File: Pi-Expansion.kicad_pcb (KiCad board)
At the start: 2 copper layers, 56 x 65 mm, 129 parts, among them J1 RPi_GPIO, J2 MMCX_H, J3 PINHEADER_2X2_SMD, P1 BATT, U1 A2200-A, U2 Racom R-78B5.0-1.5L

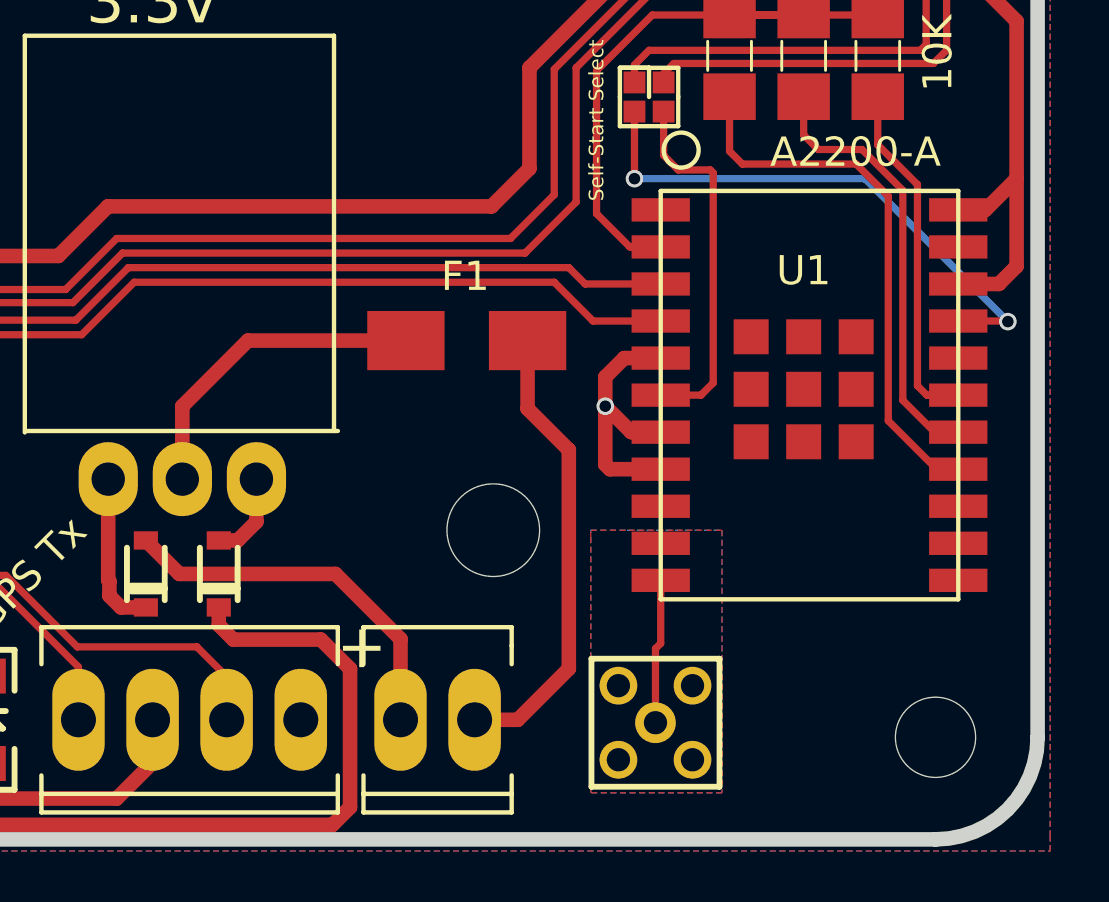
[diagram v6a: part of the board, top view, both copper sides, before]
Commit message: Added voltage select for GPS Vant between 5v and 3v3.
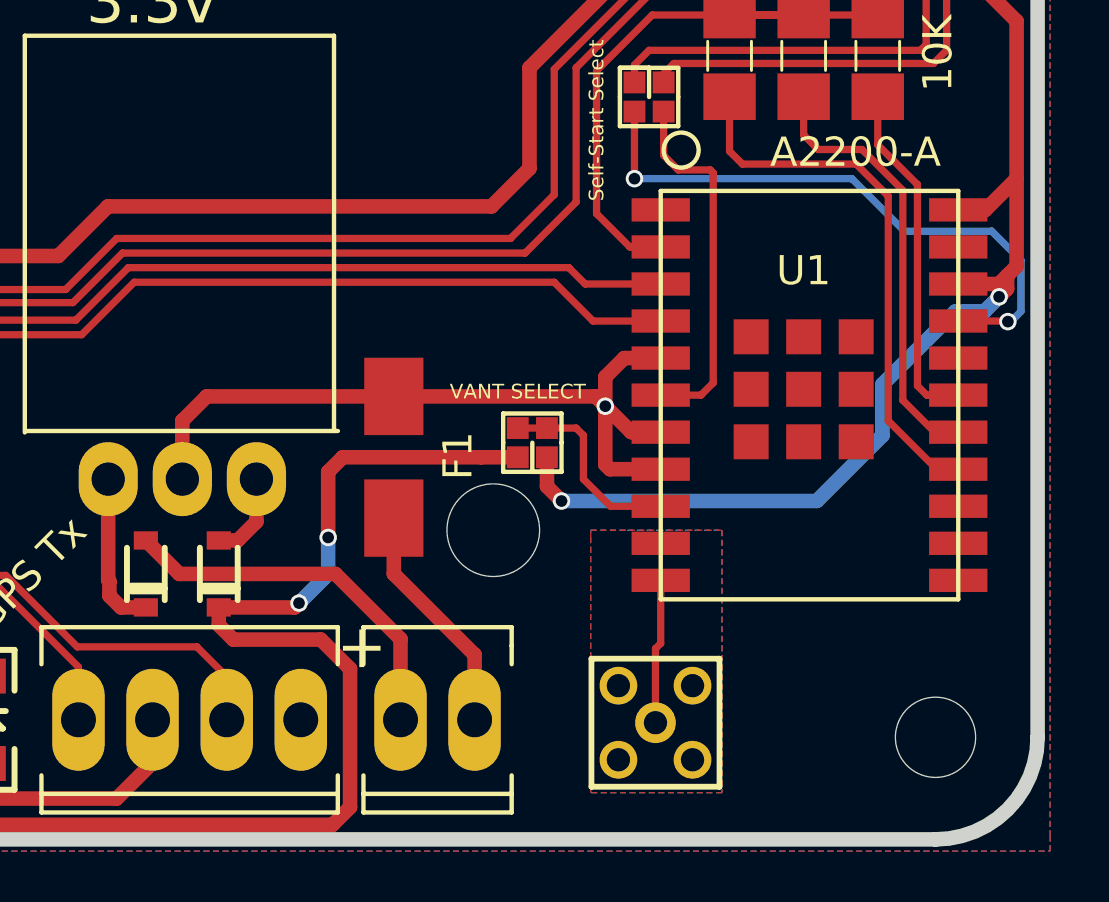
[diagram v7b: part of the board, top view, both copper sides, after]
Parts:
- added J4: PINHEADER_2X2_SMD, Sailbot_Custom:2-WAY-SMD-JUMPER, F.Cu at (106.8, 124.0)
- moved F1 4.72 mm to (102.0, 124.5), turned to 270 degrees
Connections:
- U1 pad 9: (no net) -> Net-(J4-Pad2)
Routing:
- net +3V3: track 143.7 -> 165.1 mm, vias 0 -> 2
- net +5V: track 135.3 -> 149.7 mm, vias 0 -> 2
- net Net-(F1-Pad2): track 15.8 -> 8.06 mm
- net Net-(J4-Pad2): track 0.00 -> 6.89 mm
- net GND: track 56.3 -> 62.2 mm
- net Net-(J3-Pad4): track 18.8 -> 20.8 mm

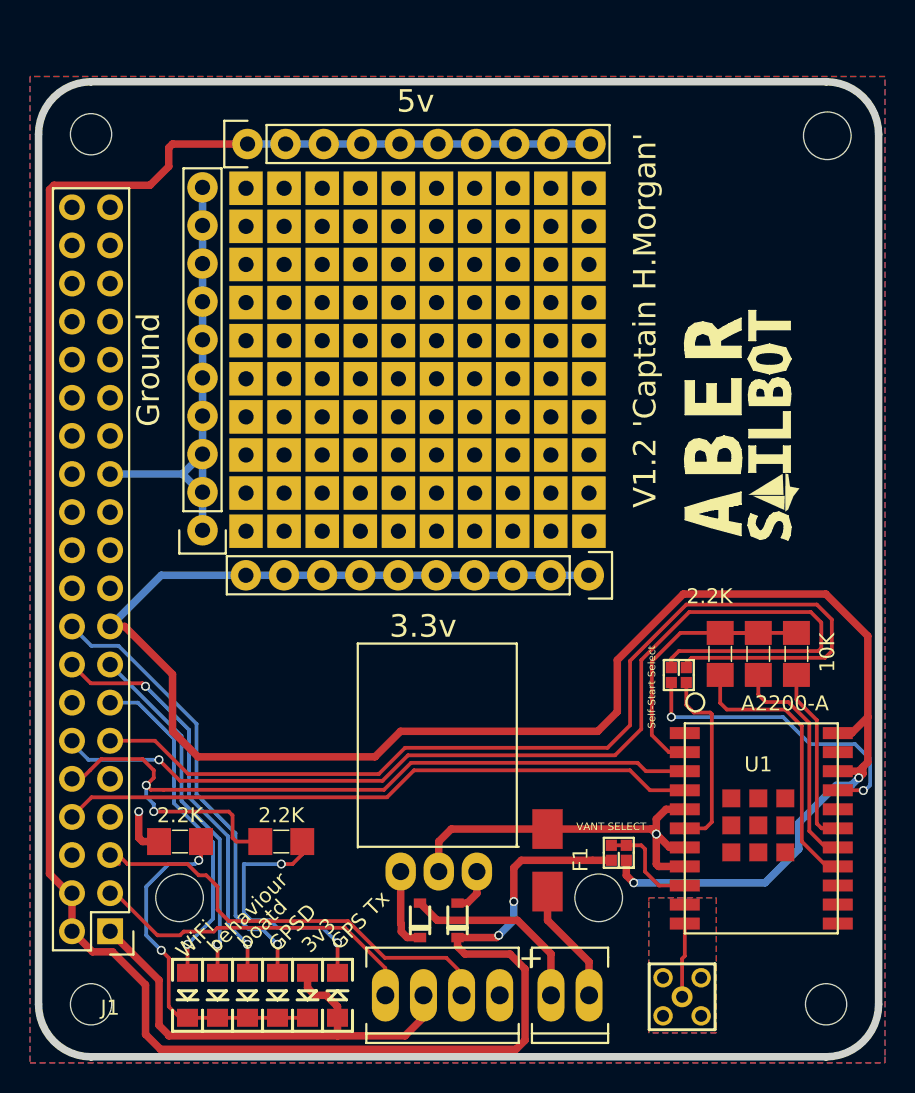
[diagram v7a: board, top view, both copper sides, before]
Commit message: Updated silkscreen typo.
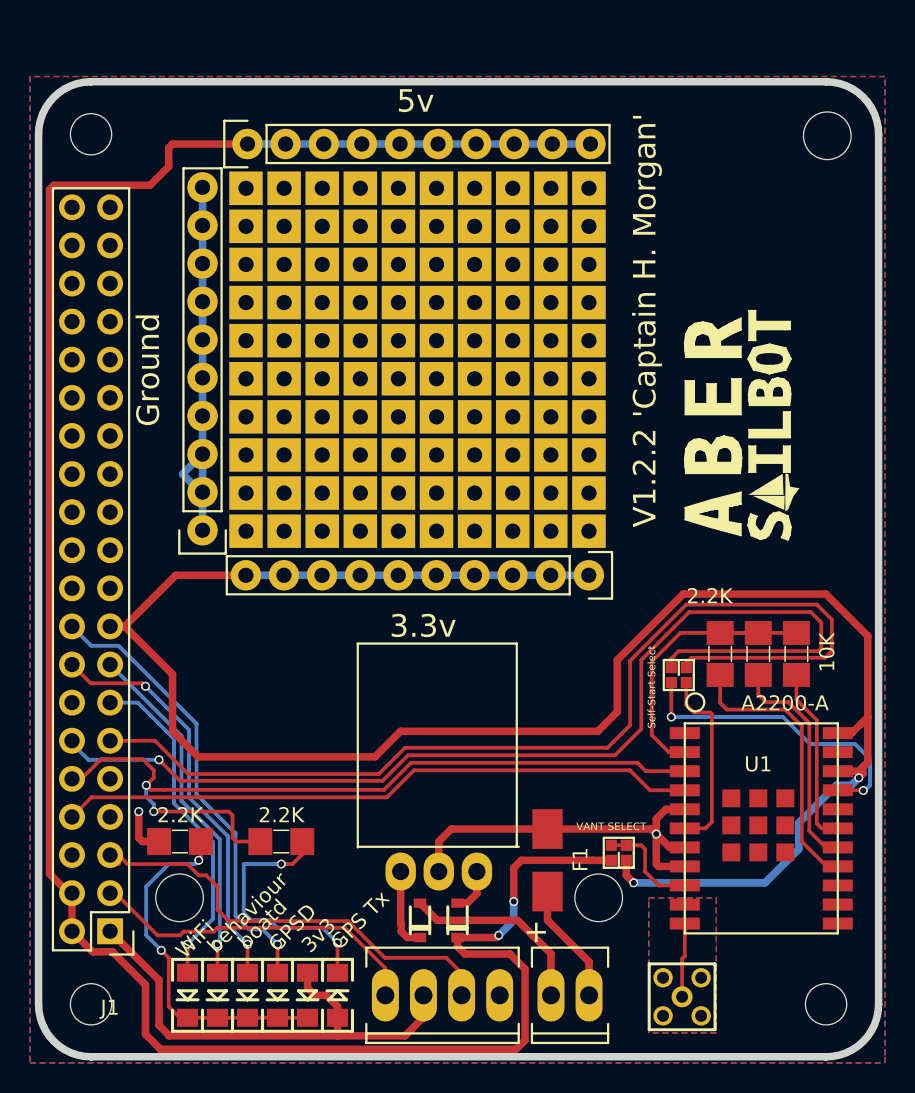
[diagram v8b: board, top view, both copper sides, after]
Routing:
- net GND: track 62.2 -> 57.4 mm
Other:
- board text added: "V1.2.2 'Captain H. Morgan'"
- board text removed: "V1.2 'Captain H.Morgan'"
